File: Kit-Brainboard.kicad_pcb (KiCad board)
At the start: 4 copper layers, 40 x 68 mm, 248 parts, among them J1 Pins_02x04_RightAngle_P2.54mm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, J2 Pins_02x05_P1.27mm_SMT, J3 USB_B_Micro_10118194-0011LF, Q1 MMBT3904, U1 PCM3060PW, U10 NJM2068, U11 NJM2068, U12 NJM2068, U13 NCP51460SN33, U14 DDR3L-RAM-4Gb_MT41K256M16TW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

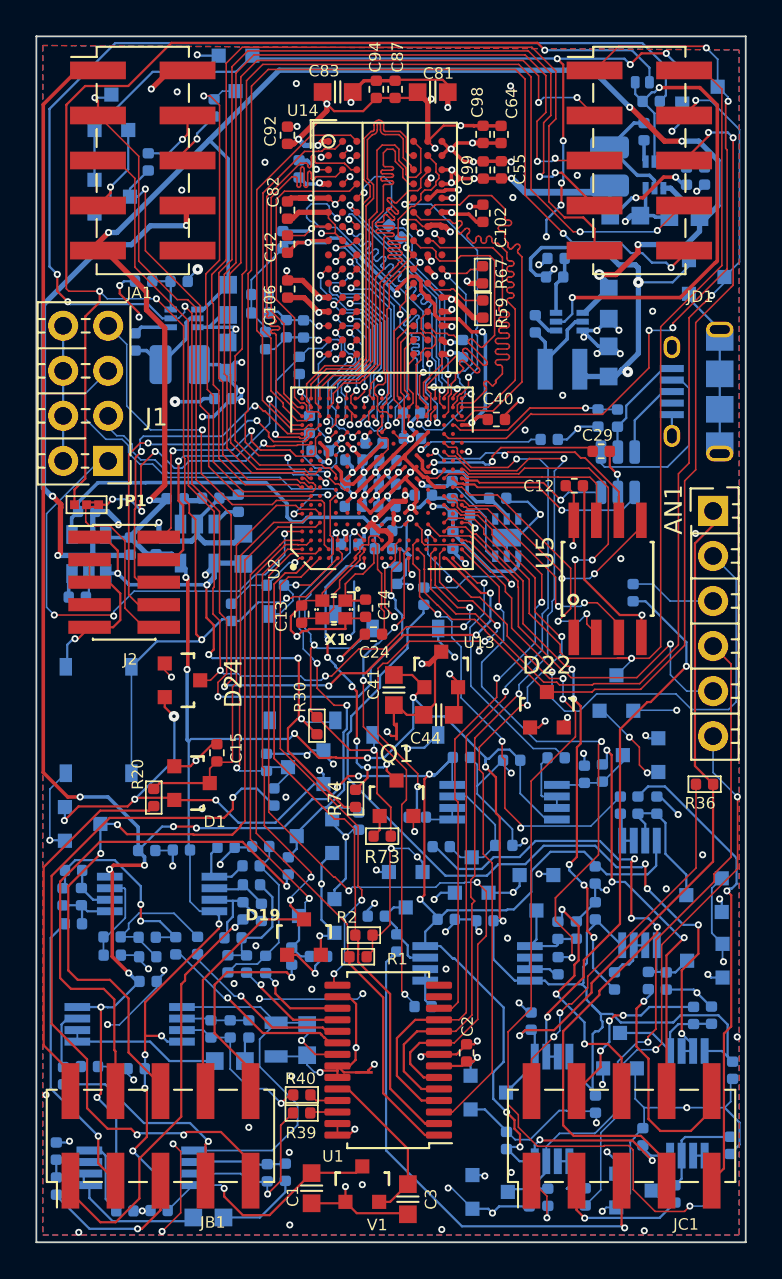
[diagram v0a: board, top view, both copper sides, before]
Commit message: Added USB pins: Changed JD4 to 2x6 header
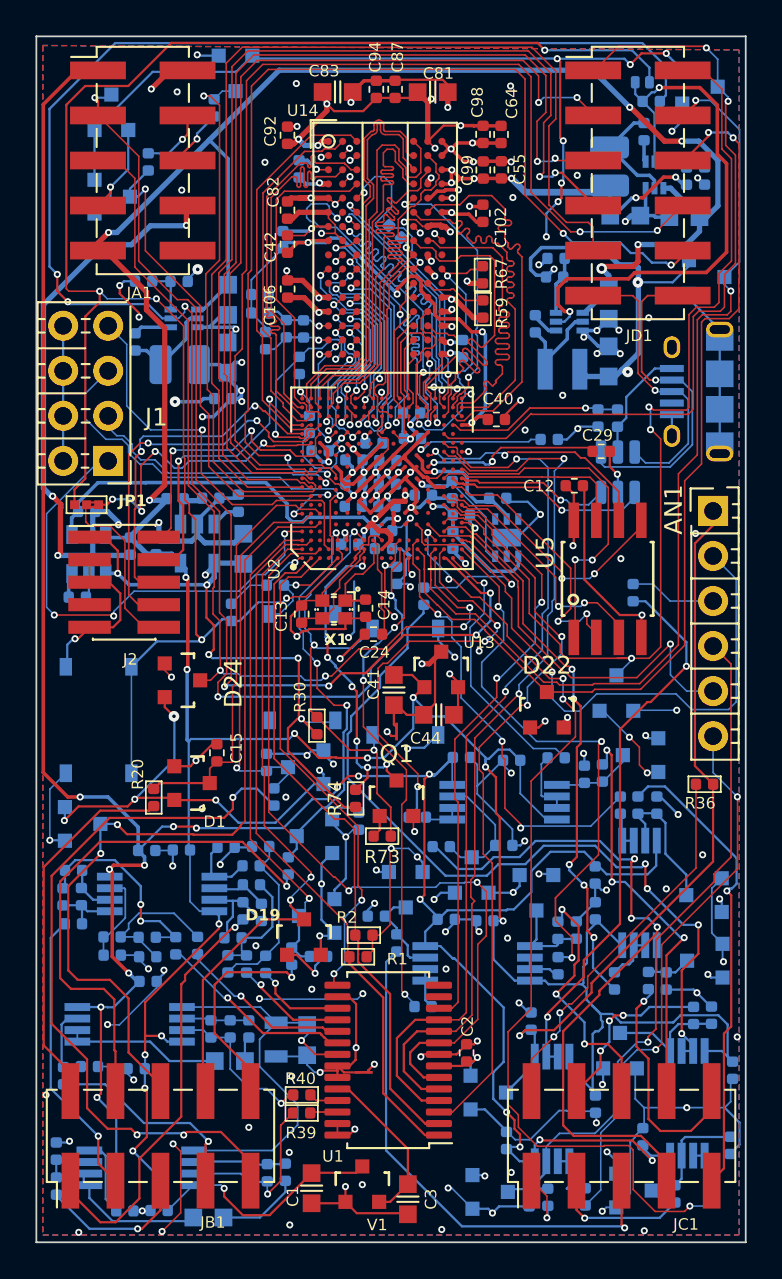
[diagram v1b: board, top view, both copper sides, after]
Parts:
- JD1: value Pins_02x05_P2.54mm_SMT -> Conn_02x06_Odd_Even; footprint Connector_PinHeader_2.54mm:PinHeader_2x05_P2.54mm_Vertical_SMD -> Connector_PinHeader_2.54mm:PinHeader_2x06_P2.54mm_Vertical_SMD
- moved JD1 1.27 mm to (223.2, 64.5)
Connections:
- J3 pad 2: Net-(J3-D-) -> USB_DM
- J3 pad 3: Net-(J3-D+) -> USB_DP
- U3 pad 4: Net-(J3-D-) -> USB_DM
- U3 pad 6: Net-(J3-D+) -> USB_DP
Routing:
- net USB_DM: track 0.00 -> 19.1 mm, vias 0 -> 1
- net USB_DP: track 0.00 -> 16.4 mm, vias 0 -> 1
- net Net-(J3-D-): track 10.1 -> 0.00 mm
- net Net-(J3-D+): track 4.08 -> 0.00 mm
- net /D5: track 41.6 -> 44.8 mm, vias 4 -> 2
- net /D6: track 53.9 -> 57.0 mm, vias 1 -> 3
- net /PWR_ONRST: track 29.7 -> 31.7 mm
- net /D8: track 53.9 -> 55.0 mm
- net /D7: track 54.1 -> 55.2 mm
- net GND: track 339.0 -> 339.1 mm, vias 153 -> 152
